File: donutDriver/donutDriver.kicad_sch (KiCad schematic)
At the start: 42 parts, among them J1 Keystone 7767, J2 Keystone 7767, J3 Keystone 7767, J4 Keystone 7767, J5 Keystone 7767, J6 Conn_Coaxial_Small, J7 Conn_Coaxial_Small, Q1 IPP320N20N3, Q2 BSS138

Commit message: begin pcb
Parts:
- C10, C11, C12, C8, C9: footprint Capacitor_THT:C_Disc_D7.5mm_W4.4mm_P5.00mm -> donutlib:TDK_Disc_D7.5mm_W5.0mm_P7.50mm
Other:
- moved on the sheet: H1, H2, H3, H4

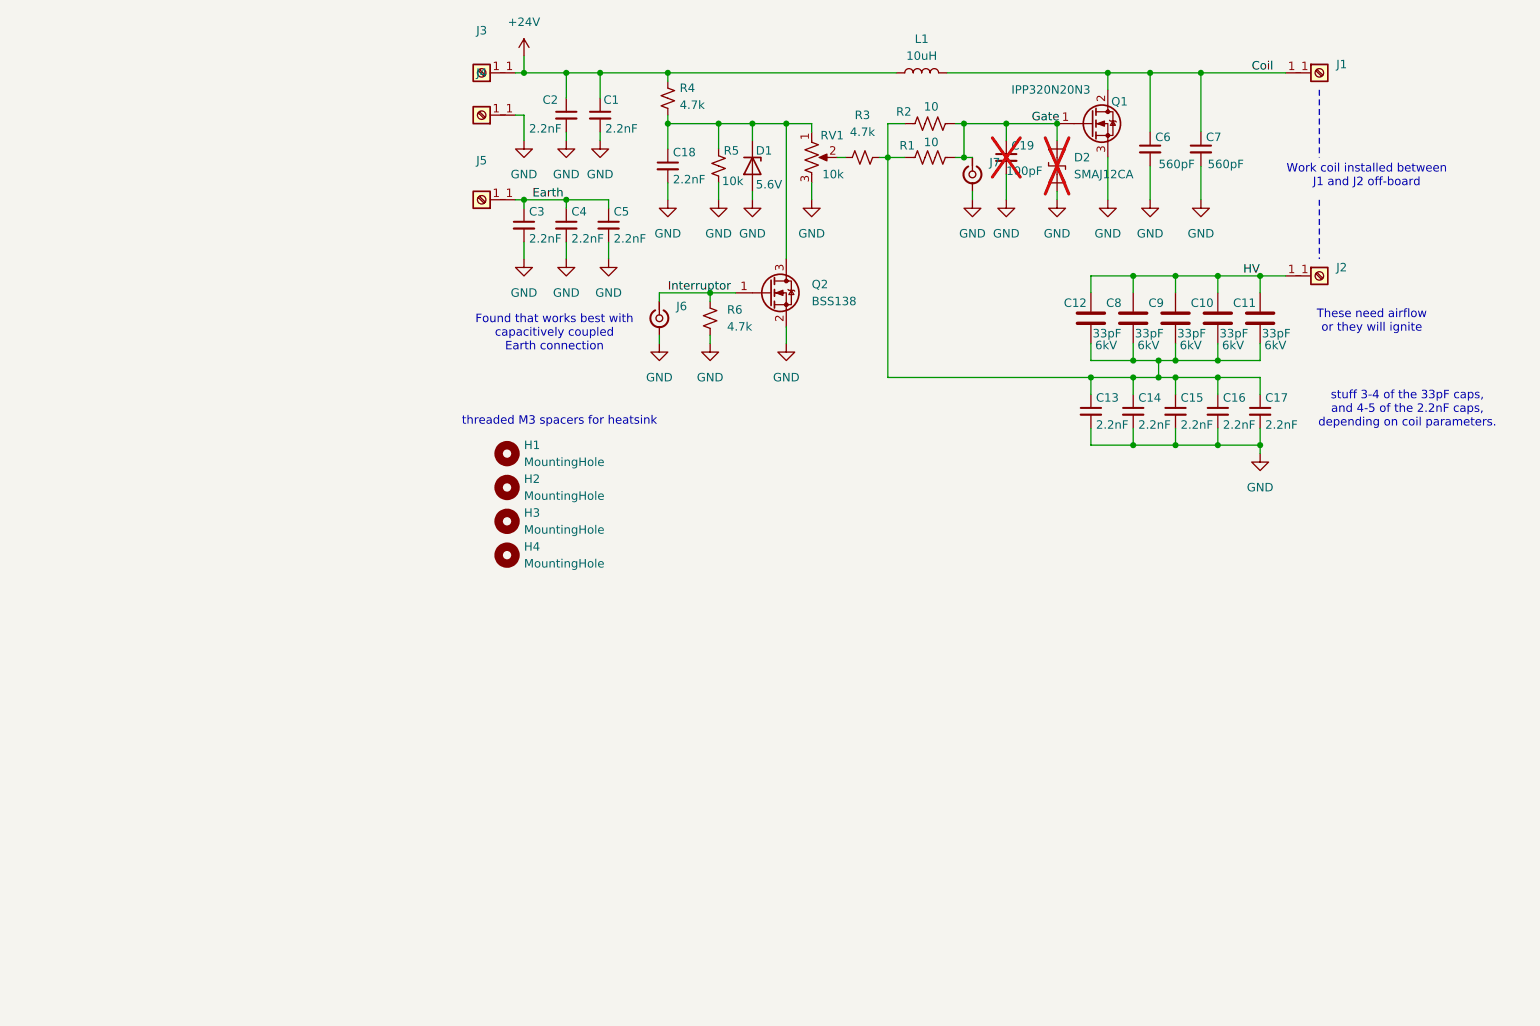
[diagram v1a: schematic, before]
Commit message: add fan switching regulator and jumpers
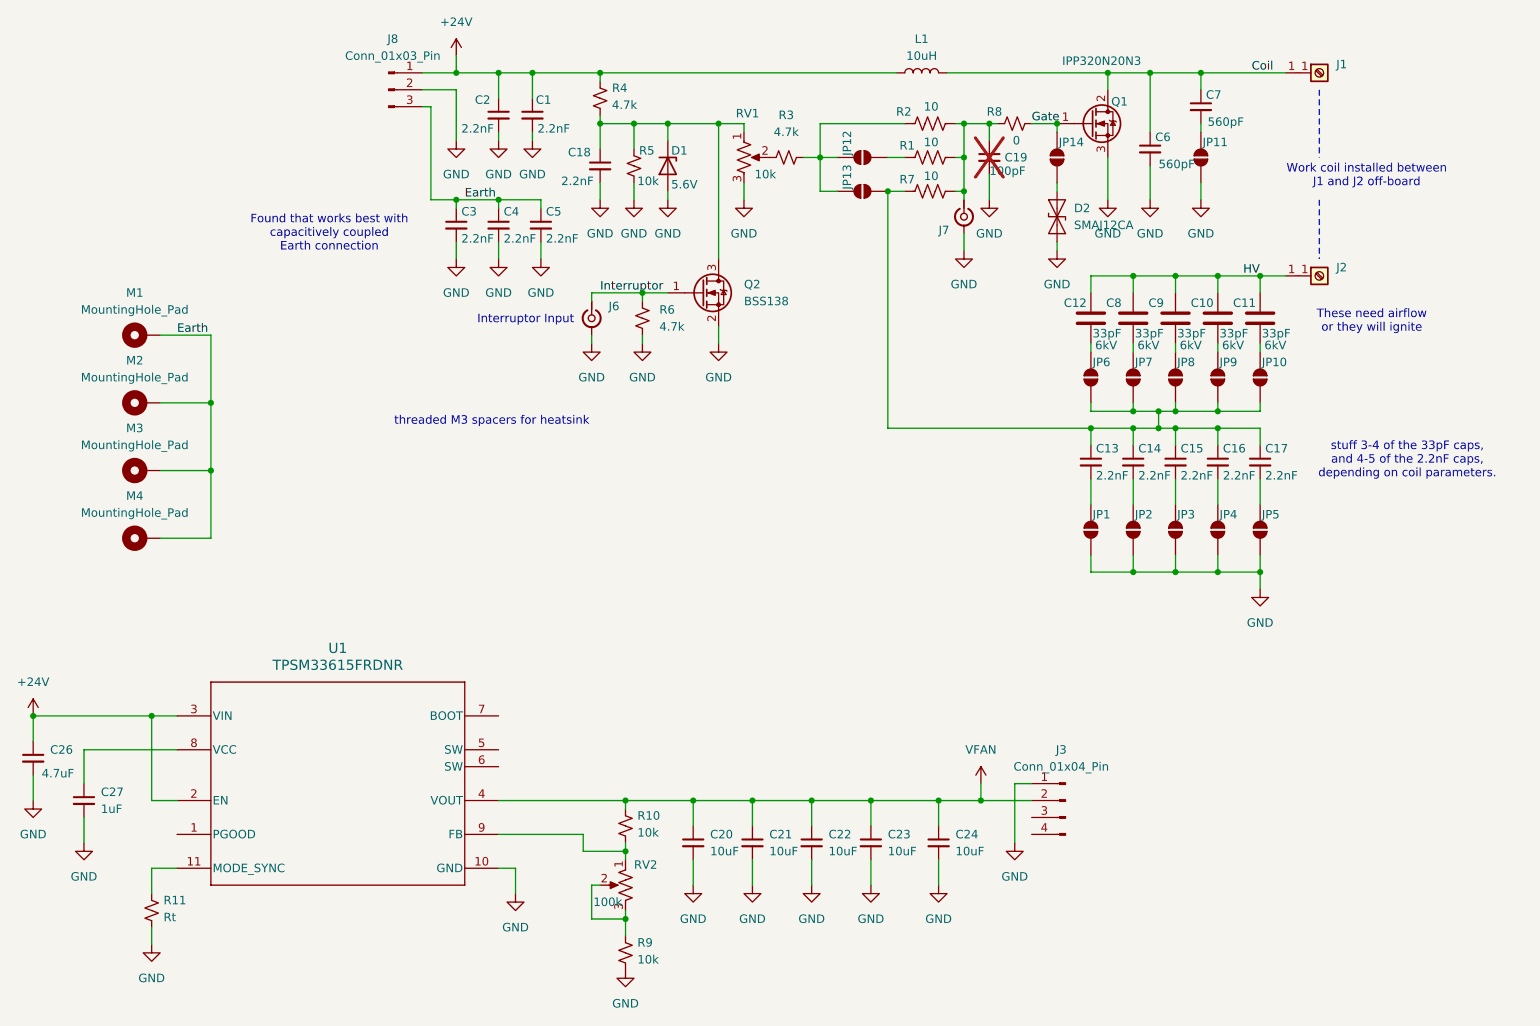
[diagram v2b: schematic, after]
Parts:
- removed H1, H2, H3, H4: MountingHole, donutlib:WA-SMSI_9774025360, symbol Mechanical:MountingHole
- removed J3, J4, J5: Keystone 7767, donutlib:KEYSTONE_7767, symbol donutlib:Keystone_7767
- added C20, C21, C22, C23, C24: 10uF, Capacitor_SMD:C_0805_2012Metric, symbol Device:C_Small
- added C26: 4.7uF, Capacitor_SMD:C_1210_3225Metric, symbol Device:C_Small
- added C27: 1uF, Capacitor_SMD:C_0603_1608Metric, symbol Device:C_Small
- added J3: Conn_01x04_Pin, Connector_JST:JST_XH_B4B-XH-A_1x04_P2.50mm_Vertical, symbol Connector:Conn_01x04_Pin
- added J8: Conn_01x03_Pin, donutlib:CONN3_2601-3103_WAG, symbol Connector:Conn_01x03_Pin
- added JP1, JP10, JP11, JP12, JP13, JP14, JP2, JP3, JP4, JP5, JP6, JP7, JP8, JP9: SolderJumper_2_Open, Jumper:SolderJumper-2_P1.3mm_Open_RoundedPad1.0x1.5mm, symbol Jumper:SolderJumper_2_Open
- added M1, M2, M3, M4: MountingHole_Pad, donutlib:WA-SMSI_9774025360, symbol Mechanical:MountingHole_Pad
- added R10, R9: 10k, Resistor_SMD:R_0603_1608Metric, symbol Device:R_Small_US
- added R11: Rt, Resistor_SMD:R_0603_1608Metric, symbol Device:R_Small_US
- added R7: 10, Resistor_SMD:R_2512_6332Metric, symbol Device:R_US
- added R8: 0, Resistor_SMD:R_1206_3216Metric, symbol Device:R_Small_US
- added RV2: 100k, Potentiometer_THT:Potentiometer_Bourns_PTV09A-2_Single_Horizontal, symbol Device:R_Potentiometer_US
- added U1: TPSM33615FRDNR, donutlib:RDN0011A-MFG, symbol donutlib:TPSM33615FRDNR
- D2: now fitted
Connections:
- net +24V: now also C26.1, J8.1 (Pin_1), U1.2 (EN), U1.3 (VIN)
- net Earth: now also J8.3 (Pin_3), M1.1, M2.1, M3.1, M4.1
- net GND: now also C20.2, C21.2, C22.2, C23.2, C24.2, C26.2, C27.2, J3.1 (Pin_1), J8.2 (Pin_2), JP1.1 (A), JP11.1 (A), JP2.1 (A), JP3.1 (A), JP4.1 (A), JP5.1 (A), R11.1, R9.1, U1.10 (GND); no longer C13.2, C14.2, C15.2, C16.2, C17.2, C7.2
- net Gate: now also JP14.2 (B), R8.2; no longer C19.1, D2.2 (A2), J7.1 (In), R1.2, R2.2
- new net: C10.2, JP9.2 (B)
- new net: C13.1, C14.1, C15.1, C16.1, C17.1, JP10.1 (A), JP13.1 (A), JP6.1 (A), JP7.1 (A), JP8.1 (A), JP9.1 (A), R7.1
- new net: C16.2, JP4.2 (B)
- new net: JP12.2 (B), JP13.2 (B), R2.1, R3.2
- new net: C19.1, J7.1 (In), R1.2, R2.2, R7.2, R8.1
- new net: R11.2, U1.11 (MODE_SYNC)
- new net: C27.1, U1.8 (VCC)
- new net: R10.1, RV2.1, U1.9 (FB)
- new net: C14.2, JP2.2 (B)
- new net: C7.2, JP11.2 (B)
- new net: C9.2, JP8.2 (B)
- new net: C12.2, JP6.2 (B)
- new net: C17.2, JP5.2 (B)
- new net: C13.2, JP1.2 (B)
- new net: C15.2, JP3.2 (B)
- new net: D2.2 (A2), JP14.1 (A)
- new net: C8.2, JP7.2 (B)
- new net: C11.2, JP10.2 (B)
- new net: R9.2, RV2.2, RV2.3
- new net: JP12.1 (A), R1.1
- new net VFAN: C20.1, C21.1, C22.1, C23.1, C24.1, J3.2 (Pin_2), R10.2, U1.4 (VOUT)
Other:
- note added: "Interruptor Input"
- moved on the sheet: C1, C13, C14, C15, C16, C17, C18, C19, C2, C3, C4, C5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
